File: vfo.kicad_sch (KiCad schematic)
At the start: 19 parts, among them Q3 2N2222A, Q4 2N2222A, Q5 2N2222A, Y1 7.2Mhz

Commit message: Rework RF amplifier design and add AF amplification
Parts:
- renumbered C11 to C17, C12 to C18, C13 to C19, C14 to C20, C15 to C21, C16 to C22, C17 to C23, R7 to R14, R8 to R15, R9 to R16, R10 to R17, R11 to R18, R12 to R19, R13 to R20, R14 to R21
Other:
- moved on the sheet: C17, C18, C19, C20, C21, C22, C23, Q3, Q4, Q5, R14, R15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

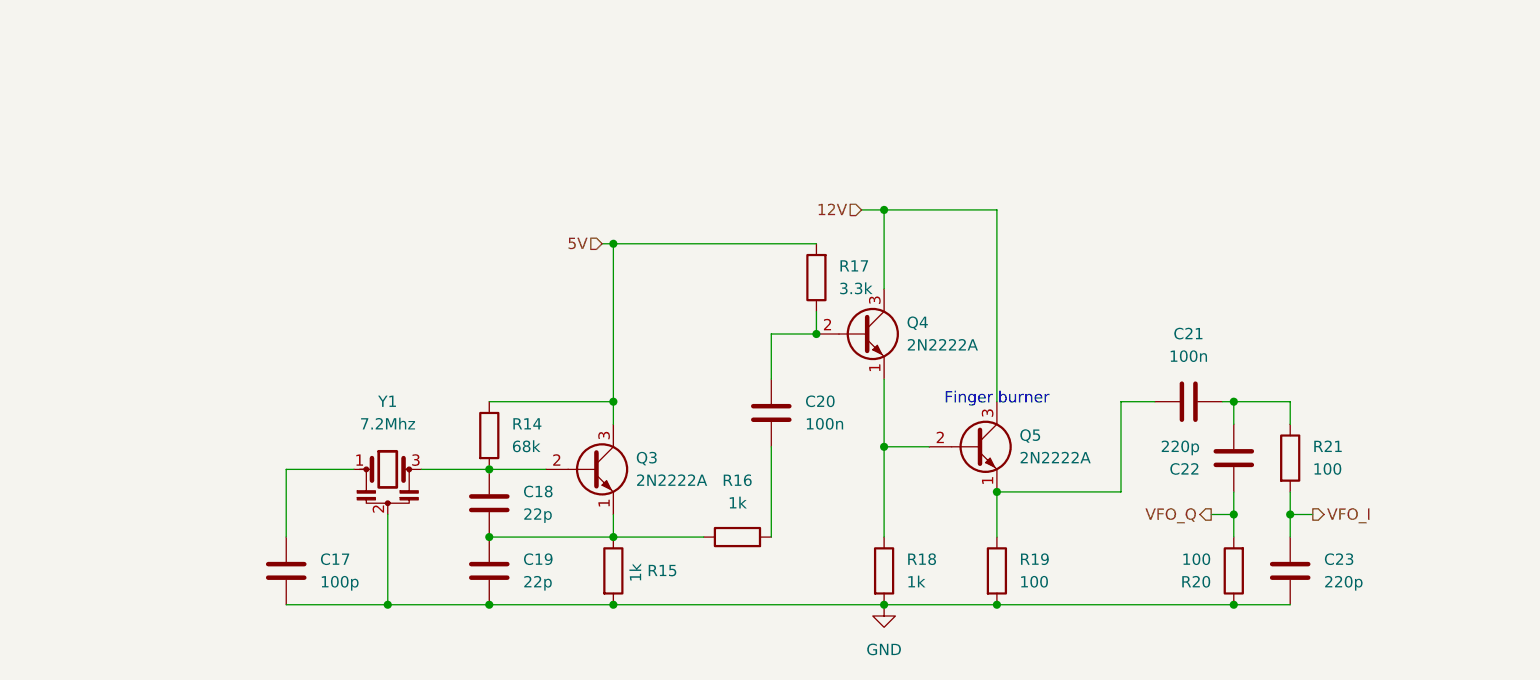
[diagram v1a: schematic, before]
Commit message: Add more gain fix crystal oscillator starting, add audio isolation transformers
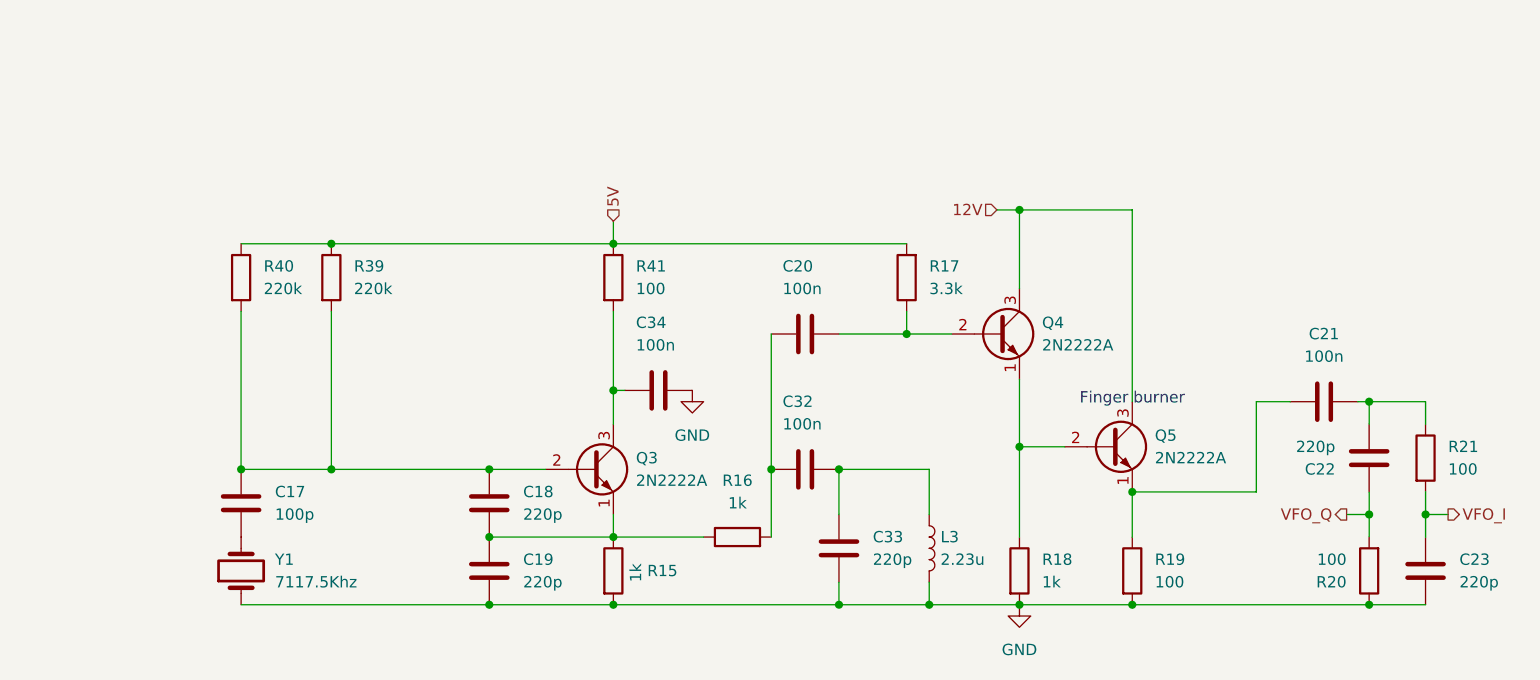
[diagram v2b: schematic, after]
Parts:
- removed R14: 68k, symbol Device:R
- removed Y1: 7.2Mhz, symbol Device:Resonator
- added C32, C34: 100n, symbol Device:C
- added C33: 220p, symbol Device:C
- added L3: 2.23u, symbol Device:L
- added R39, R40: 220k, symbol Device:R
- added R41: 100, symbol Device:R
- added Y1: 7117.5Khz, symbol Device:Crystal
- C18, C19: value 22p -> 220p
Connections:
- net 5V: now also R39.1, R40.1, R41.1; no longer Q3.3 (C)
- net GND: now also C33.2, C34.1, L3.2, Y1.1; no longer C17.2
- net at C18.1, Q3.2 (B): now also C17.1, R39.2, R40.2
- net at Q4.2 (B), R17.1: now also C20.1; no longer C20.2
- net at R16.2: now also C20.2, C32.2; no longer C20.1
- new net: C34.2, Q3.3 (C), R41.2
- new net: C17.2, Y1.2
- new net: C32.1, C33.1, L3.1
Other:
- moved on the sheet: C17, C20, C21, C22, C23, Q4, Q5, R17, R18, R19, R20, R21
